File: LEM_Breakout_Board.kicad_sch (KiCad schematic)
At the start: 5 parts, among them J1 Conn_01x06_Male, J2 Conn_01x04_Female

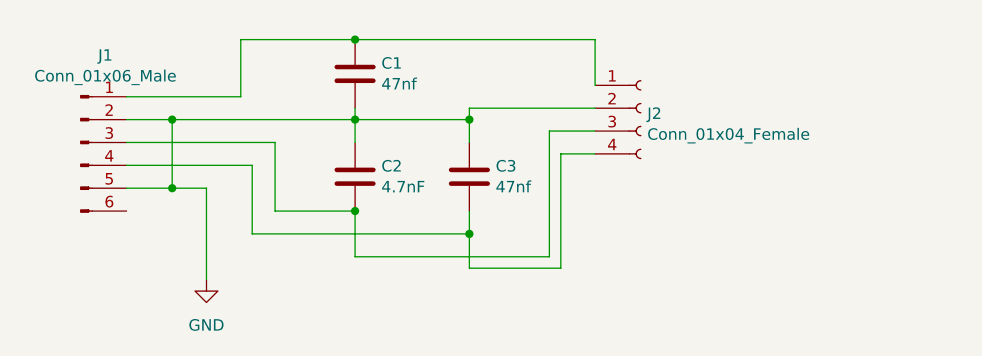
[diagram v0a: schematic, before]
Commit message: Updated layout for Grove Connector
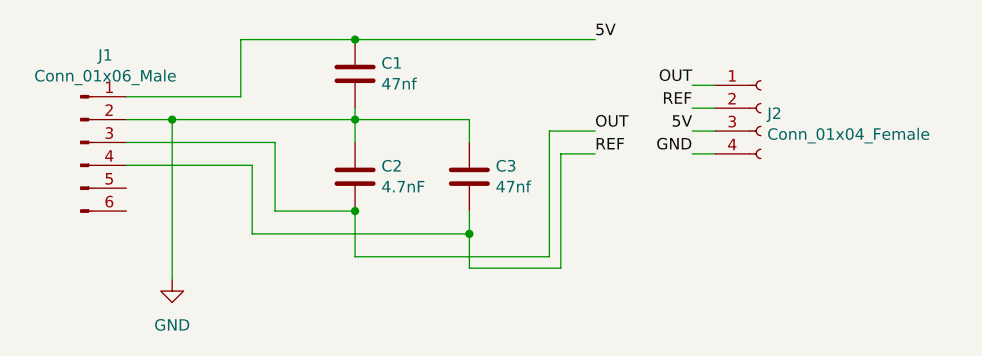
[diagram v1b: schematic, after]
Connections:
- net GND: now also J2.4 (Pin_4); no longer J1.5 (Pin_5), J2.2 (Pin_2)
- net 5V: now reaches C1.1, J1.1 (Pin_1)
- net 5V: now also J2.3 (Pin_3); no longer J2.1 (Pin_1)
- net OUT: now reaches C2.2, J1.3 (Pin_3)
- net OUT: now also J2.1 (Pin_1); no longer J2.3 (Pin_3)
- net REF: now reaches C3.2, J1.4 (Pin_4)
- net REF: now also J2.2 (Pin_2); no longer J2.4 (Pin_4)
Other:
- moved on the sheet: J2

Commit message: Started Redesign
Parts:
- removed J1: Conn_01x06_Male, user:LEM_HAIS_50-P, symbol Connector:Conn_01x06_Male
- added D1: LED, LED_SMD:LED_0603_1608Metric, symbol Device:LED
- added D2, D3: D_Schottky_Dual_Series_ACK, Package_TO_SOT_SMD:SOT-23, symbol Device:D_Schottky_Dual_Series_ACK
- added F1: Polyfuse, Fuse:Fuse_0603_1608Metric, symbol Device:Polyfuse
- added R1, R2, R3, R4, R5: R, Resistor_SMD:R_0603_1608Metric, symbol Device:R
- added U*1: LEM HO 60-P 0100, Sensor_Current:LEM_HO40-NP, symbol Connector_Generic:Conn_01x09
- C1, C2, C3: footprint Capacitor_THT:C_Disc_D3.4mm_W2.1mm_P2.50mm -> Capacitor_SMD:C_0603_1608Metric
- J2: footprint Connector_PinHeader_2.00mm:PinHeader_1x04_P2.00mm_Vertical -> Connector_JST:JST_PH_S4B-PH-SM4-TB_1x04-1MP_P2.00mm_Horizontal
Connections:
- net GND: now also C2.2, C3.2, D2.1 (A), D3.1 (A), R1.2, U*1.2 (Pin_2); no longer C2.1, C3.1
- net 5V renamed +5V
- net +5V: now also F1.1; no longer C1.1
- net OUT renamed Sense_Output
- net Sense_Output: now also R4.2; no longer C2.2
- net REF renamed Ref_Output
- net Ref_Output: now also R5.2; no longer C3.2
- new net: D1.1 (K), R1.1
- new net 5V_Fused: C1.1, D1.2 (A), D2.3 (K), D3.3 (K), F1.2, U*1.1 (Pin_1)
- new net OCD: U*1.5 (Pin_5)
- new net Ref: C3.1, R3.1, U*1.4 (Pin_4)
- new net Ref_Mid: D3.2 (common), R3.2, R5.1
- new net Sense: C2.1, R2.1, U*1.3 (Pin_3)
- new net Sense_Mid: D2.2 (common), R2.2, R4.1
- no-connect marks 0 -> 4
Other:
- moved on the sheet: C1, C2, C3, J2

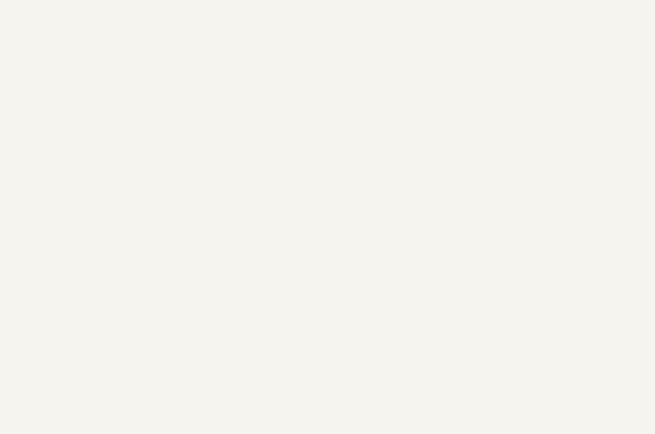
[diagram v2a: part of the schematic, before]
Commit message: Redesign for LEM HO 60-P
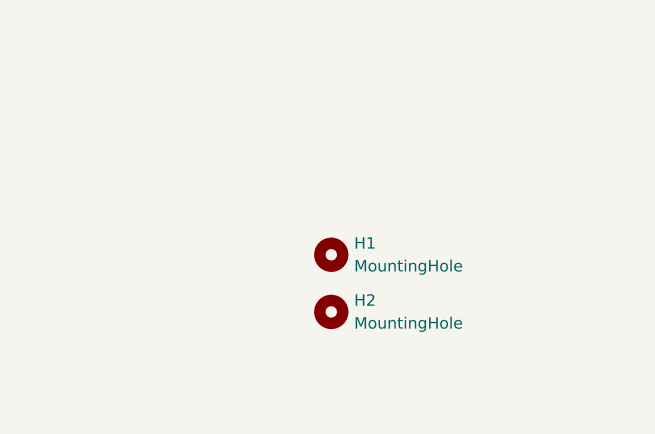
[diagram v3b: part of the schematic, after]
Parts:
- added H1, H2: MountingHole, MountingHole:MountingHole_3.2mm_M3_DIN965, symbol Mechanical:MountingHole
- C1, C3: LCSC (none) -> C1622
- C2: LCSC (none) -> C53987
- R4, R5: footprint Resistor_SMD:R_0603_1608Metric -> Resistor_SMD:R_0805_2012Metric
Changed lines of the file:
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@@
+			)
+		)
+		(property "LCSC" "C1622"
+			(at 121.031 40.7416 0)
+			(effects
+				(font
+					(size 1.27 1.27)
+				)
+				(hide yes)
 			)
 		)
@@
 			)
 		)
+		(property "LCSC" "C53987"
+			(at 117.221 78.8416 0)
+			(effects
+				(font
+					(size 1.27 1.27)
+				)
+				(hide yes)
+			)
+		)
 		(pin "1"
 		)
@@
 					(size 1.27 1.27)
 				)
+			)
+		)
+		(property "LCSC" "C1622"
+			(at 128.651 78.8416 0)
+			(effects
+				(font
+					(size 1.27 1.27)
+				)
+				(hide yes)
 			)
 		)
@@
 	)
 	(symbol
+		(lib_id "Mechanical:MountingHole")
+		(at 181.61 116.84 0)
+		(unit 1)
+		(body_style 1)
+		(exclude_from_sim no)
+		(in_bom no)
+		(on_board yes)
+		(in_pos_files yes)
+		(dnp no)
+		(fields_autoplaced yes)
+		(property "Reference" "H2"
+			(at 184.15 115.57 0)
+			(show_name no)
+			(do_not_autoplace no)
+			(effects
+				(font
+					(size 1.27 1.27)
+				)
+				(justify left)
+			)
+		)
+		(property "Value" "MountingHole"
+			(at 184.15 118.11 0)
+			(show_name no)
+			(do_not_autoplace no)
+			(effects
+				(font
+					(size 1.27 1.27)
+				)
+				(justify left)
+			)
+		)
+		(property "Footprint" "MountingHole:MountingHole_3.2mm_M3_DIN965"
+			(at 181.61 116.84 0)
+			(hide yes)
+			(show_name no)
+			(do_not_autoplace no)
+			(effects
+				(font
+					(size 1.27 1.27)
+				)
+			)
+		)
+		(property "Datasheet" ""
+			(at 181.61 116.84 0)
+			(hide yes)
+			(show_name no)
+			(do_not_autoplace no)
+			(effects
+				(font
+					(size 1.27 1.27)
+				)
+			)
+		)
+		(property "Description" "Mounting Hole without connection"
+			(at 181.61 116.84 0)
+			(hide yes)
+			(show_name no)
+			(do_not_autoplace no)
+			(effects
+				(font
+					(size 1.27 1.27)
+				)
+			)
+		)
+		(instances
+			(project "LEM_Breakout_Board"
+				(path "/cbc539d2-6a10-4052-9b7a-f10326dcac67"
+					(reference "H2")
+					(unit 1)
+				)
+			)
+		)
+	)
+	(symbol
 		(lib_id "Device:R")
 		(at 134.62 74.93 90)
@@
 			)
 		)
-		(property "Footprint" "Resistor_SMD:R_0603_1608Metric"
+		(property "Footprint" "Resistor_SMD:R_0805_2012Metric"
 			(at 153.67 73.152 90)
 			(hide yes)
@@
 				(path "/cbc539d2-6a10-4052-9b7a-f10326dcac67"
 					(reference "R5")
+					(unit 1)
+				)
+			)
+		)
+	)
+	(symbol
+		(lib_id "Mechanical:MountingHole")
+		(at 181.61 110.49 0)
+		(unit 1)
+		(body_style 1)
+		(exclude_from_sim no)
+		(in_bom no)
+		(on_board yes)
+		(in_pos_files yes)
+		(dnp no)
+		(fields_autoplaced yes)
+		(property "Reference" "H1"
+			(at 184.15 109.22 0)
+			(show_name no)
+			(do_not_autoplace no)
+			(effects
+				(font
+					(size 1.27 1.27)
+				)
+				(justify left)
+			)
+		)
+		(property "Value" "MountingHole"
+			(at 184.15 111.76 0)
+			(show_name no)
+			(do_not_autoplace no)
+			(effects
+				(font
+					(size 1.27 1.27)
+				)
+				(justify left)
+			)
+		)
+		(property "Footprint" "MountingHole:MountingHole_3.2mm_M3_DIN965"
+			(at 181.61 110.49 0)
+			(hide yes)
+			(show_name no)
+			(do_not_autoplace no)
+			(effects
+				(font
+					(size 1.27 1.27)
+				)
+			)
+		)
+		(property "Datasheet" ""
+			(at 181.61 110.49 0)
+			(hide yes)
+			(show_name no)
+			(do_not_autoplace no)
+			(effects
+				(font
+					(size 1.27 1.27)
+				)
+			)
+		)
+		(property "Description" "Mounting Hole without connection"
+			(at 181.61 110.49 0)
+			(hide yes)
+			(show_name no)
+			(do_not_autoplace no)
+			(effects
+				(font
+					(size 1.27 1.27)
+				)
+			)
+		)
+		(instances
+			(project "LEM_Breakout_Board"
+				(path "/cbc539d2-6a10-4052-9b7a-f10326dcac67"
+					(reference "H1")
 					(unit 1)
 				)
@@
 			)
 		)
-		(property "Footprint" "Resistor_SMD:R_0603_1608Metric"
+		(property "Footprint" "Resistor_SMD:R_0805_2012Metric"
 			(at 153.67 72.898 90)
 			(hide yes)

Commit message: Changed LED Footprint to 0805
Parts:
- D1: footprint LED_SMD:LED_0603_1608Metric -> LED_SMD:LED_0805_2012Metric
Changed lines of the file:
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@@
 		(property "LCSC" "C1622"
 			(at 121.031 40.7416 0)
-			(effects
-				(font
-					(size 1.27 1.27)
-				)
-				(hide yes)
+			(hide yes)
+			(show_name no)
+			(do_not_autoplace no)
+			(effects
+				(font
+					(size 1.27 1.27)
+				)
 			)
 		)
@@
 		(property "LCSC" "C53987"
 			(at 117.221 78.8416 0)
-			(effects
-				(font
-					(size 1.27 1.27)
-				)
-				(hide yes)
+			(hide yes)
+			(show_name no)
+			(do_not_autoplace no)
+			(effects
+				(font
+					(size 1.27 1.27)
+				)
 			)
 		)
@@
 		(property "LCSC" "C1622"
 			(at 128.651 78.8416 0)
-			(effects
-				(font
-					(size 1.27 1.27)
-				)
-				(hide yes)
+			(hide yes)
+			(show_name no)
+			(do_not_autoplace no)
+			(effects
+				(font
+					(size 1.27 1.27)
+				)
 			)
 		)
@@
 			)
 		)
-		(property "Footprint" "LED_SMD:LED_0603_1608Metric"
+		(property "Footprint" "LED_SMD:LED_0805_2012Metric"
 			(at 128.27 36.83 0)
 			(hide yes)
